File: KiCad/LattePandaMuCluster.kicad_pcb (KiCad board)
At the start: 2 copper layers, 203.2 x 170.2 mm, 723 parts, among them J1 ATX-24, J10 Bus_M.2_Socket_M, J11 Bus_M.2_Socket_M, J12 Bus_M.2_Socket_M, J13 Bus_M.2_Socket_M, J14 Bus_M.2_Socket_M, J15 Conn_01x04, J16 Conn_01x05, J17 Conn_01x04, J18 Conn_01x04, J19 RJ45_LED_Shielded_x2, J2 Conn_02x04_Top_Bottom, J20 RJE361882415, J21 RJ45_LED_Shielded_x2, J22 USB3_A_Stacked, J23 USB3_IDC, J24 Conn_01x04, J25 Conn_01x05, J26 HDMI_A, J27 JACK-USBE-20PINTL, J3 SFF-8087, J4 SFF-8087, J5 SATA, J6 Bus_M.2_Socket_E, J7 Bus_M.2_Socket_E, J8 Bus_PCI_Express_x4, J9 Bus_PCI_Express_x4, M1 Fan_4pin, M10 Fan_4pin, M2 Fan_4pin, M3 Fan_4pin, M4 Fan_4pin, M5 Fan_4pin, M6 Fan_4pin, M7 Fan_4pin, M8 Fan_4pin, M9 Fan_4pin, Q1 2N7002, Q2 2N7002, Q3 2N7002, U1 ZD25Q64BSIGT, U10 H5VU25U, U11 H5VU25U, U12 KTI226V, U13 KTI226V, U14 ZD25Q64BSIGT, U15 ZD25Q64BSIGT, U16 H5VU25U, U17 H5VU25U, U18 H5VU25U, U19 H5VU25U, U2 ZD25Q64BSIGT, U20 KTI226V, U21 KTI226V, U22 ZD25Q64BSIGT, U23 ZD25Q64BSIGT, U24 H5VU25U, U25 H5VU25U, U26 KTI226V, U27 ZD25Q64BSIGT, U28 H5VU25U, U29 H5VU25U, U3 ZD25Q64BSIGT, U30 H5VU25U, U31 H5VU25U, U32 H5VU25U, U33 H5VU25U, U34 H5VU25U, U35 H5VU25U, U36 H5VU25U, U37 H5VU25U, U38 H5VU25U, U39 H5VU25U, U4 ZD25Q64BSIGT, U40 TPS65987DDJRSHR, U41 H5VU25U, U42 H5VU25U, U43 ZD25Q64BSIGT, U44 H5VU25U, U5 ZD25Q64BSIGT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

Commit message: Arranging components
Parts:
- H10, H11, H7, H8, H9: moved to B.Cu
- moved TR5 309.4 mm to (204.0, 180.0), turned to 180 degrees
- moved TR4 297.7 mm to (188.0, 180.0), turned to 180 degrees
- moved U26 295.9 mm to (204.0, 165.0), turned to 180 degrees
- moved TR3 286.9 mm to (172.0, 180.0), turned to 180 degrees
- moved U21 283.5 mm to (188.0, 165.0), turned to 180 degrees
- moved TR2 277.2 mm to (156.0, 180.0), turned to 180 degrees
- moved U20 271.7 mm to (172.0, 165.0), turned to 180 degrees
- moved TR1 268.5 mm to (140.0, 180.0), turned to 180 degrees
- moved U13 260.7 mm to (156.0, 165.0), turned to 180 degrees
- moved U12 250.7 mm to (140.0, 165.0), turned to 180 degrees
- moved H5 234.1 mm to (253.0, 175.0)
- moved H6 233.4 mm to (253.0, 200.0)
- moved H11 225.9 mm to (239.0, 80.0), turned to 180 degrees
- moved J6 223.0 mm to (223.0, 175.0), turned to 90 degrees
- moved J7 222.1 mm to (223.0, 200.0), turned to 90 degrees
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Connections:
- net /Module 1/TYPE_C_HEADER.SBU1 renamed /Module 1/TYPE_C_HEADER.SBU2
- J19 pad 1: Net-(TR2-MX1+) -> Net-(TR2-MX4-)
- J19 pad 13: Net-(TR3-MX1+) -> Net-(TR3-MX4-)
- J19 pad 14: Net-(TR3-MX1-) -> Net-(TR3-MX4+)
- J19 pad 15: Net-(TR3-MX2+) -> Net-(TR3-MX3-)
- J19 pad 16: Net-(TR3-MX3+) -> Net-(TR3-MX2-)
- J19 pad 17: Net-(TR3-MX3-) -> Net-(TR3-MX2+)
- J19 pad 18: Net-(TR3-MX2-) -> Net-(TR3-MX3+)
- J19 pad 19: Net-(TR3-MX4+) -> Net-(TR3-MX1-)
- J19 pad 2: Net-(TR2-MX1-) -> Net-(TR2-MX4+)
- J19 pad 20: Net-(TR3-MX4-) -> Net-(TR3-MX1+)
- J19 pad 3: Net-(TR2-MX2+) -> Net-(TR2-MX3-)
- J19 pad 4: Net-(TR2-MX3+) -> Net-(TR2-MX2-)
- J19 pad 5: Net-(TR2-MX3-) -> Net-(TR2-MX2+)
- J19 pad 6: Net-(TR2-MX2-) -> Net-(TR2-MX3+)
- J19 pad 7: Net-(TR2-MX4+) -> Net-(TR2-MX1-)
- J19 pad 8: Net-(TR2-MX4-) -> Net-(TR2-MX1+)
- J20 pad 1: Net-(TR1-MX1+) -> Net-(TR1-MX4-)
- J20 pad 2: Net-(TR1-MX1-) -> Net-(TR1-MX4+)
- J20 pad 3: Net-(TR1-MX2+) -> Net-(TR1-MX3-)
- J20 pad 4: Net-(TR1-MX3+) -> Net-(TR1-MX2-)
- J20 pad 5: Net-(TR1-MX3-) -> Net-(TR1-MX2+)
- J20 pad 6: Net-(TR1-MX2-) -> Net-(TR1-MX3+)
- J20 pad 7: Net-(TR1-MX4+) -> Net-(TR1-MX1-)
- J20 pad 8: Net-(TR1-MX4-) -> Net-(TR1-MX1+)
- J21 pad 1: Net-(TR4-MX1+) -> Net-(TR4-MX4-)
- J21 pad 13: Net-(TR5-MX1+) -> Net-(TR5-MX4-)
- J21 pad 14: Net-(TR5-MX1-) -> Net-(TR5-MX4+)
- J21 pad 15: Net-(TR5-MX2+) -> Net-(TR5-MX3-)
- J21 pad 16: Net-(TR5-MX3+) -> Net-(TR5-MX2-)
- J21 pad 17: Net-(TR5-MX3-) -> Net-(TR5-MX2+)
- J21 pad 18: Net-(TR5-MX2-) -> Net-(TR5-MX3+)
- J21 pad 19: Net-(TR5-MX4+) -> Net-(TR5-MX1-)
- J21 pad 2: Net-(TR4-MX1-) -> Net-(TR4-MX4+)
- J21 pad 20: Net-(TR5-MX4-) -> Net-(TR5-MX1+)
- J21 pad 3: Net-(TR4-MX2+) -> Net-(TR4-MX3-)
- J21 pad 4: Net-(TR4-MX3+) -> Net-(TR4-MX2-)
- J21 pad 5: Net-(TR4-MX3-) -> Net-(TR4-MX2+)
- J21 pad 6: Net-(TR4-MX2-) -> Net-(TR4-MX3+)
- J21 pad 7: Net-(TR4-MX4+) -> Net-(TR4-MX1-)
- J21 pad 8: Net-(TR4-MX4-) -> Net-(TR4-MX1+)
- TR1 pad 15: Net-(R128-Pad1) -> Net-(R131-Pad1)
- TR1 pad 18: Net-(R129-Pad1) -> Net-(R130-Pad1)
- TR1 pad 21: Net-(R130-Pad1) -> Net-(R129-Pad1)
- TR1 pad 24: Net-(R131-Pad1) -> Net-(R128-Pad1)
- TR2 pad 15: Net-(R132-Pad1) -> Net-(R135-Pad1)
- TR2 pad 18: Net-(R133-Pad1) -> Net-(R134-Pad1)
- TR2 pad 21: Net-(R134-Pad1) -> Net-(R133-Pad1)
- TR2 pad 24: Net-(R135-Pad1) -> Net-(R132-Pad1)
- TR3 pad 15: Net-(R162-Pad1) -> Net-(R165-Pad1)
- TR3 pad 18: Net-(R163-Pad1) -> Net-(R164-Pad1)
- TR3 pad 21: Net-(R164-Pad1) -> Net-(R163-Pad1)
- TR3 pad 24: Net-(R165-Pad1) -> Net-(R162-Pad1)
- TR4 pad 15: Net-(R166-Pad1) -> Net-(R169-Pad1)
- TR4 pad 18: Net-(R167-Pad1) -> Net-(R168-Pad1)
- TR4 pad 21: Net-(R168-Pad1) -> Net-(R167-Pad1)
- TR4 pad 24: Net-(R169-Pad1) -> Net-(R166-Pad1)
- TR5 pad 15: Net-(R190-Pad1) -> Net-(R193-Pad1)
- TR5 pad 18: Net-(R191-Pad1) -> Net-(R192-Pad1)
- TR5 pad 21: Net-(R192-Pad1) -> Net-(R191-Pad1)
- TR5 pad 24: Net-(R193-Pad1) -> Net-(R190-Pad1)
- U10 pad 1: Net-(TR2-TD4-) -> Net-(TR2-TD1+)
- U10 pad 2: Net-(TR2-TD4+) -> Net-(TR2-TD1-)
- U10 pad 4: Net-(TR2-TD3+) -> Net-(TR2-TD2-)
- U10 pad 5: Net-(TR2-TD3-) -> Net-(TR2-TD2+)
- U11 pad 1: Net-(TR2-TD2-) -> Net-(TR2-TD3+)
- U11 pad 2: Net-(TR2-TD2+) -> Net-(TR2-TD3-)
- U11 pad 4: Net-(TR2-TD1+) -> Net-(TR2-TD4-)
- U11 pad 5: Net-(TR2-TD1-) -> Net-(TR2-TD4+)
- U12 pad 45: Net-(TR1-TD1+) -> Net-(TR1-TD4-)
- U12 pad 46: Net-(TR1-TD1-) -> Net-(TR1-TD4+)
- U12 pad 48: Net-(TR1-TD2+) -> Net-(TR1-TD3-)
- U12 pad 49: Net-(TR1-TD2-) -> Net-(TR1-TD3+)
- U12 pad 51: Net-(TR1-TD3+) -> Net-(TR1-TD2-)
- U12 pad 52: Net-(TR1-TD3-) -> Net-(TR1-TD2+)
- U12 pad 54: Net-(TR1-TD4+) -> Net-(TR1-TD1-)
- U12 pad 55: Net-(TR1-TD4-) -> Net-(TR1-TD1+)
- U13 pad 45: Net-(TR2-TD1+) -> Net-(TR2-TD4-)
- U13 pad 46: Net-(TR2-TD1-) -> Net-(TR2-TD4+)
- U13 pad 48: Net-(TR2-TD2+) -> Net-(TR2-TD3-)
- U13 pad 49: Net-(TR2-TD2-) -> Net-(TR2-TD3+)
- U13 pad 51: Net-(TR2-TD3+) -> Net-(TR2-TD2-)
- U13 pad 52: Net-(TR2-TD3-) -> Net-(TR2-TD2+)
- U13 pad 54: Net-(TR2-TD4+) -> Net-(TR2-TD1-)
- U13 pad 55: Net-(TR2-TD4-) -> Net-(TR2-TD1+)
- U16 pad 1: Net-(TR3-TD4-) -> Net-(TR3-TD1+)
- U16 pad 2: Net-(TR3-TD4+) -> Net-(TR3-TD1-)
- U16 pad 4: Net-(TR3-TD3+) -> Net-(TR3-TD2-)
- U16 pad 5: Net-(TR3-TD3-) -> Net-(TR3-TD2+)
- U17 pad 1: Net-(TR3-TD2-) -> Net-(TR3-TD3+)
- U17 pad 2: Net-(TR3-TD2+) -> Net-(TR3-TD3-)
- U17 pad 4: Net-(TR3-TD1+) -> Net-(TR3-TD4-)
- U17 pad 5: Net-(TR3-TD1-) -> Net-(TR3-TD4+)
- U18 pad 1: Net-(TR4-TD4-) -> Net-(TR4-TD1+)
- U18 pad 2: Net-(TR4-TD4+) -> Net-(TR4-TD1-)
- U18 pad 4: Net-(TR4-TD3+) -> Net-(TR4-TD2-)
- U18 pad 5: Net-(TR4-TD3-) -> Net-(TR4-TD2+)
- U19 pad 1: Net-(TR4-TD2-) -> Net-(TR4-TD3+)
- U19 pad 2: Net-(TR4-TD2+) -> Net-(TR4-TD3-)
- U19 pad 4: Net-(TR4-TD1+) -> Net-(TR4-TD4-)
- U19 pad 5: Net-(TR4-TD1-) -> Net-(TR4-TD4+)
- U20 pad 45: Net-(TR3-TD1+) -> Net-(TR3-TD4-)
- U20 pad 46: Net-(TR3-TD1-) -> Net-(TR3-TD4+)
- U20 pad 48: Net-(TR3-TD2+) -> Net-(TR3-TD3-)
- U20 pad 49: Net-(TR3-TD2-) -> Net-(TR3-TD3+)
- U20 pad 51: Net-(TR3-TD3+) -> Net-(TR3-TD2-)
- U20 pad 52: Net-(TR3-TD3-) -> Net-(TR3-TD2+)
- U20 pad 54: Net-(TR3-TD4+) -> Net-(TR3-TD1-)
- U20 pad 55: Net-(TR3-TD4-) -> Net-(TR3-TD1+)
- U21 pad 45: Net-(TR4-TD1+) -> Net-(TR4-TD4-)
- U21 pad 46: Net-(TR4-TD1-) -> Net-(TR4-TD4+)
- U21 pad 48: Net-(TR4-TD2+) -> Net-(TR4-TD3-)
- U21 pad 49: Net-(TR4-TD2-) -> Net-(TR4-TD3+)
- U21 pad 51: Net-(TR4-TD3+) -> Net-(TR4-TD2-)
- U21 pad 52: Net-(TR4-TD3-) -> Net-(TR4-TD2+)
- U21 pad 54: Net-(TR4-TD4+) -> Net-(TR4-TD1-)
- U21 pad 55: Net-(TR4-TD4-) -> Net-(TR4-TD1+)
- U24 pad 1: Net-(TR5-TD4-) -> Net-(TR5-TD1+)
- U24 pad 2: Net-(TR5-TD4+) -> Net-(TR5-TD1-)
- U24 pad 4: Net-(TR5-TD3+) -> Net-(TR5-TD2-)
- U24 pad 5: Net-(TR5-TD3-) -> Net-(TR5-TD2+)
- U25 pad 1: Net-(TR5-TD2-) -> Net-(TR5-TD3+)
- U25 pad 2: Net-(TR5-TD2+) -> Net-(TR5-TD3-)
- U25 pad 4: Net-(TR5-TD1+) -> Net-(TR5-TD4-)
- U25 pad 5: Net-(TR5-TD1-) -> Net-(TR5-TD4+)
- U26 pad 45: Net-(TR5-TD1+) -> Net-(TR5-TD4-)
- U26 pad 46: Net-(TR5-TD1-) -> Net-(TR5-TD4+)
- U26 pad 48: Net-(TR5-TD2+) -> Net-(TR5-TD3-)
- U26 pad 49: Net-(TR5-TD2-) -> Net-(TR5-TD3+)
- U26 pad 51: Net-(TR5-TD3+) -> Net-(TR5-TD2-)
- U26 pad 52: Net-(TR5-TD3-) -> Net-(TR5-TD2+)
- U26 pad 54: Net-(TR5-TD4+) -> Net-(TR5-TD1-)
- U26 pad 55: Net-(TR5-TD4-) -> Net-(TR5-TD1+)
- U8 pad 1: Net-(TR1-TD4-) -> Net-(TR1-TD1+)
- U8 pad 2: Net-(TR1-TD4+) -> Net-(TR1-TD1-)
- U8 pad 4: Net-(TR1-TD3+) -> Net-(TR1-TD2-)
- U8 pad 5: Net-(TR1-TD3-) -> Net-(TR1-TD2+)
- U9 pad 1: Net-(TR1-TD2-) -> Net-(TR1-TD3+)
- U9 pad 2: Net-(TR1-TD2+) -> Net-(TR1-TD3-)
- U9 pad 4: Net-(TR1-TD1+) -> Net-(TR1-TD4-)
- U9 pad 5: Net-(TR1-TD1-) -> Net-(TR1-TD4+)

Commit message: reposition nix for better space use (maybe)
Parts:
- moved U27 311.7 mm to (234.1, 138.1), turned to 180 degrees
- moved U5 305.1 mm to (236.9, 123.1), turned to 90 degrees
- moved U4 284.4 mm to (206.9, 122.6), turned to 90 degrees
- moved U23 284.1 mm to (204.1, 138.1), turned to 180 degrees
- moved U22 258.3 mm to (175.0, 138.5), turned to 180 degrees
- moved U15 232.6 mm to (145.1, 138.6), turned to 180 degrees
- moved U14 209.3 mm to (116.1, 139.0), turned to 180 degrees
- moved U1 175.9 mm to (117.1, 123.1), turned to 90 degrees
- moved U3 164.3 mm to (176.9, 122.6), turned to 90 degrees
- moved U2 146.1 mm to (146.9, 123.1), turned to 90 degrees
- moved U26 34.9 mm to (234.4, 147.9)
- moved U12 29.0 mm to (115.9, 148.9)
- moved U21 23.3 mm to (204.1, 148.1)
- moved U13 19.8 mm to (144.9, 148.6)
- moved U20 16.7 mm to (175.1, 148.6)
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
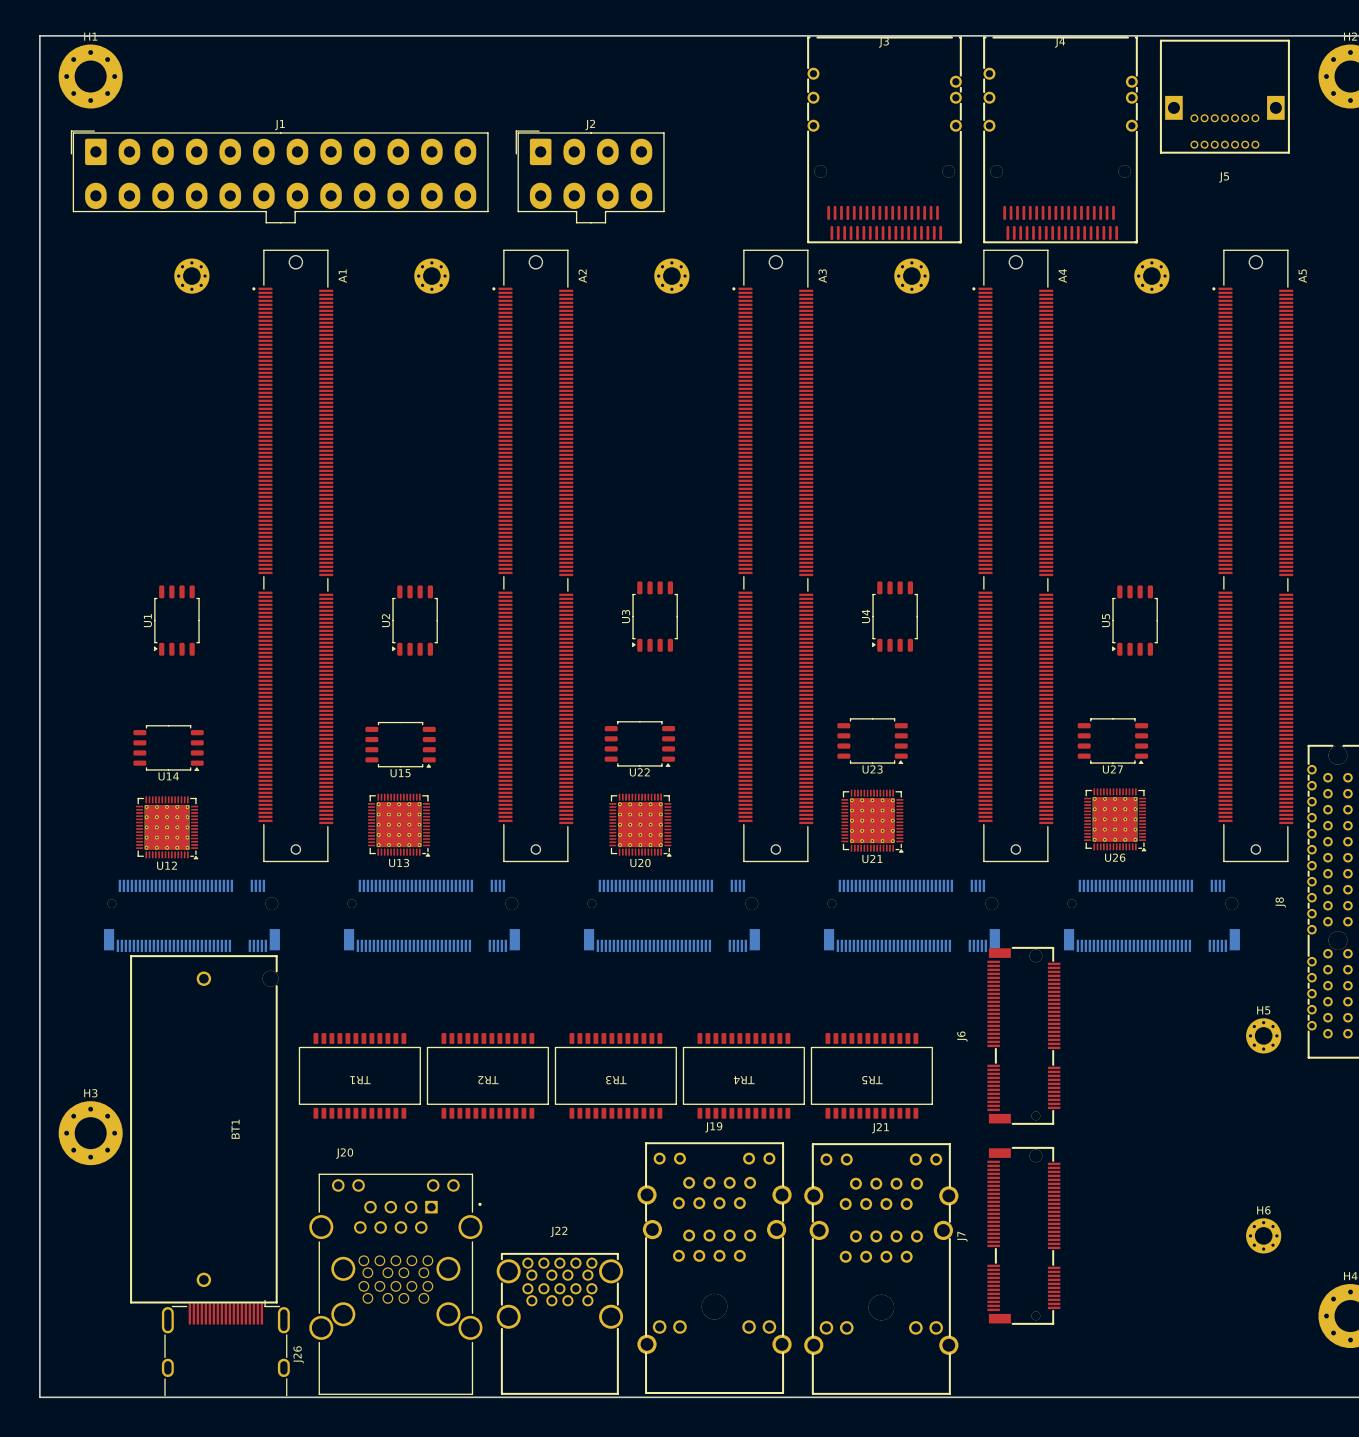
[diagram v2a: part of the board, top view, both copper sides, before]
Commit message: Move slots down to make more room for top io
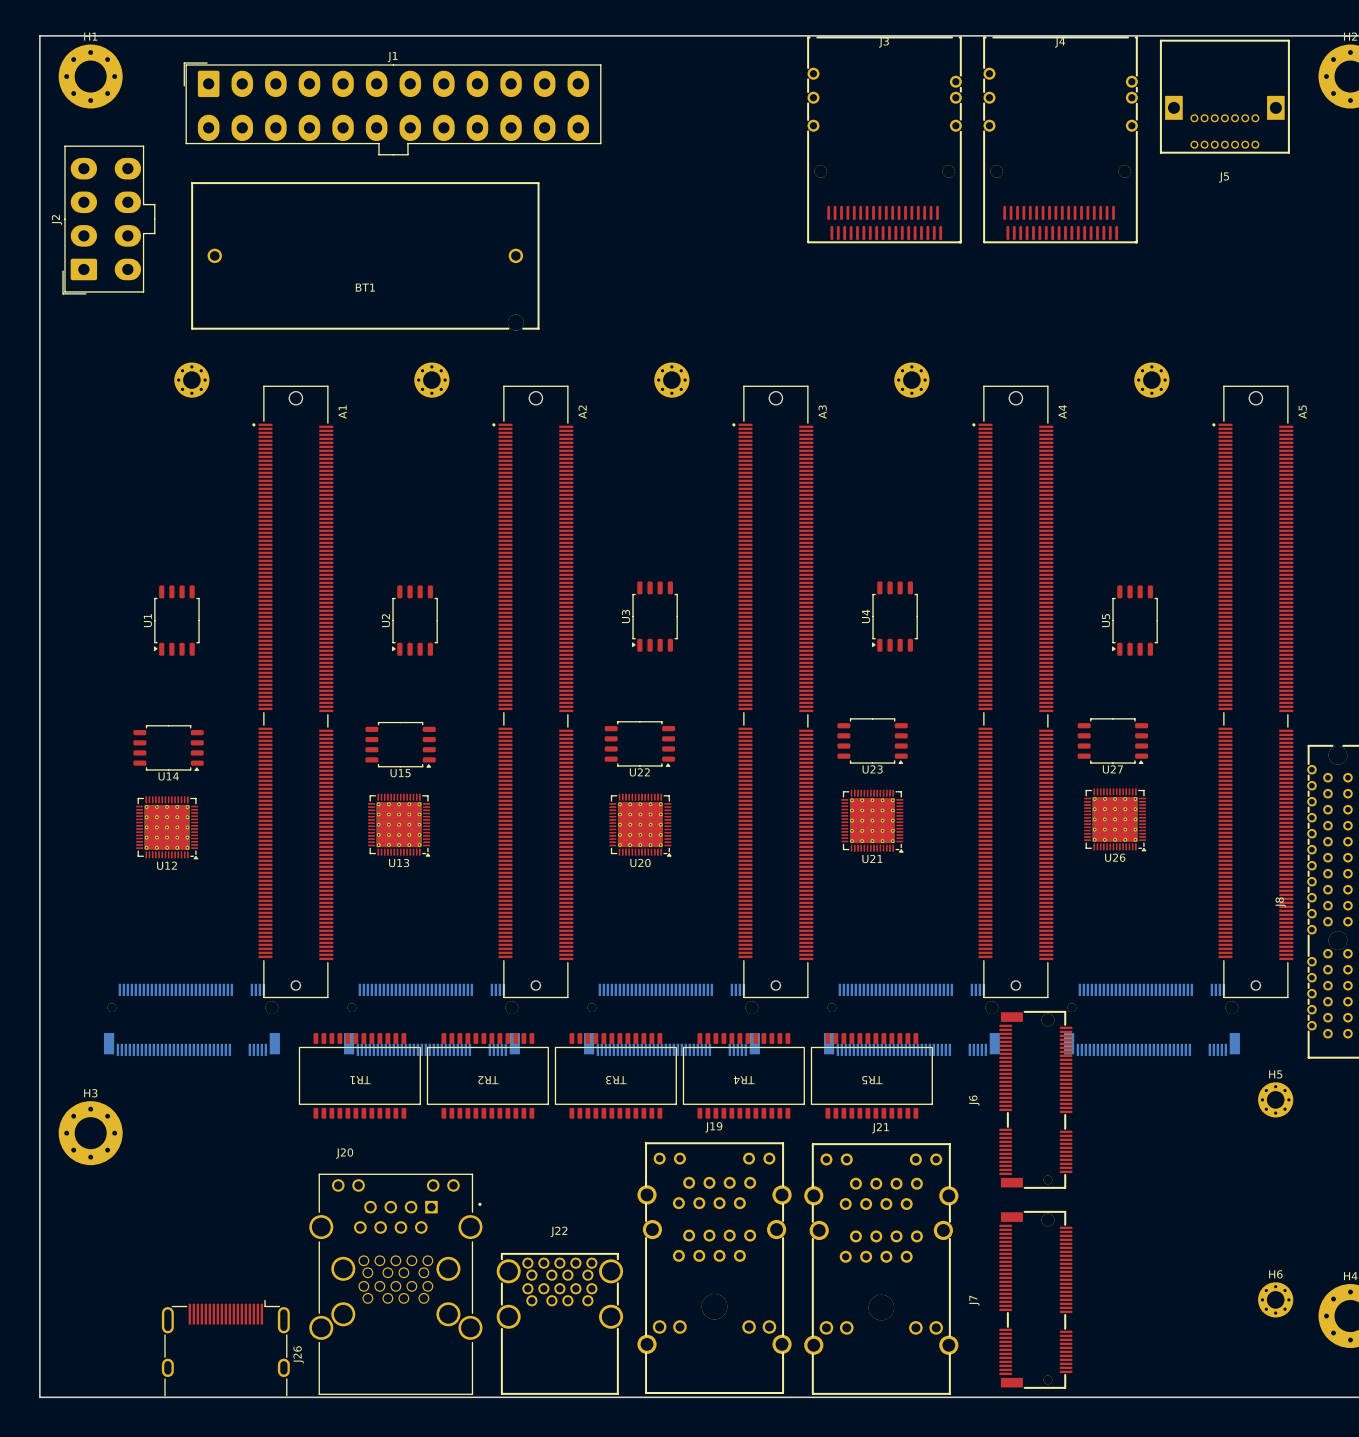
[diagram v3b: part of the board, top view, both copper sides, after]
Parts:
- moved BT1 111.0 mm to (140.7, 77.5), turned to 180 degrees
- moved J2 59.0 mm to (105.5, 79.2), turned to 90 degrees
- moved A1 17.0 mm to (132.0, 132.0)
- moved A2 17.0 mm to (162.0, 132.0)
- moved A3 17.0 mm to (192.0, 132.0)
- moved A4 17.0 mm to (222.0, 132.0)
- moved A5 17.0 mm to (252.0, 132.0)
- moved J1 16.5 mm to (121.1, 56.0)
- moved H10 13.0 mm to (209.0, 93.0)
- moved H11 13.0 mm to (239.0, 93.0)
- moved H7 13.0 mm to (119.0, 93.0)
- moved H8 13.0 mm to (149.0, 93.0)
- moved H9 13.0 mm to (179.0, 93.0)
- moved J10 13.0 mm to (119.0, 173.0)
- moved J11 13.0 mm to (149.0, 173.0)
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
